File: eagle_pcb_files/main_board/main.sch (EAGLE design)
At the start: 19 parts

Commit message: Temporary version of main board
:')
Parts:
- added C1, C2, C3, C4, C5, C6, C7: (no value), rcl:C-EUC0402
- added U$3, U$9: POLOLU_FUEL_GAUGEBREAKBOARD, SparFun-FuelGauge:POLOLU_FUEL_GAUGEBREAKBOARD
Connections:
- net 3.3V: now also C1.2, C2.1, C3.1, C4.1, C5.2, C6.1, C7.1, U$3.VCC, U$9.VCC
- net B2: now also RAO2.GPIO6
- net GND: now also C1.1, C2.2, C3.2, C4.2, C5.1, C6.2, C7.2, U$3.-, U$3.GND, U$9.-, U$9.GND
- net SCL: now also U$3.SCL, U$9.SCL
- net SDA: now also U$3.SDA, U$9.SDA
- net VIN1: now also U$3.+
- net VIN2: now also U$9.+

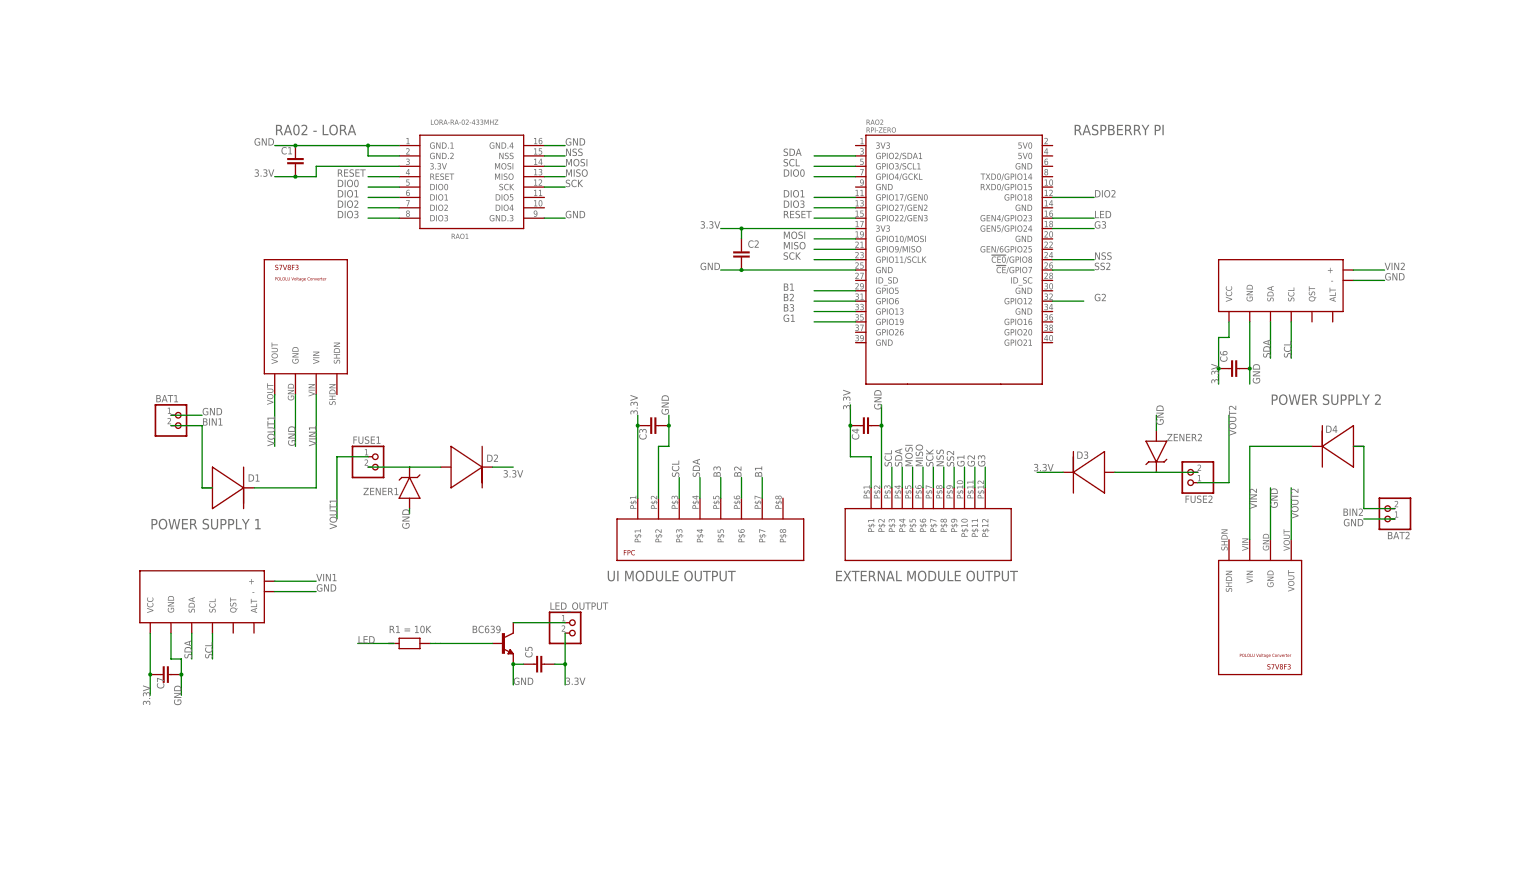
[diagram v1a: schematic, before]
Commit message: Bit better schematic
more readable
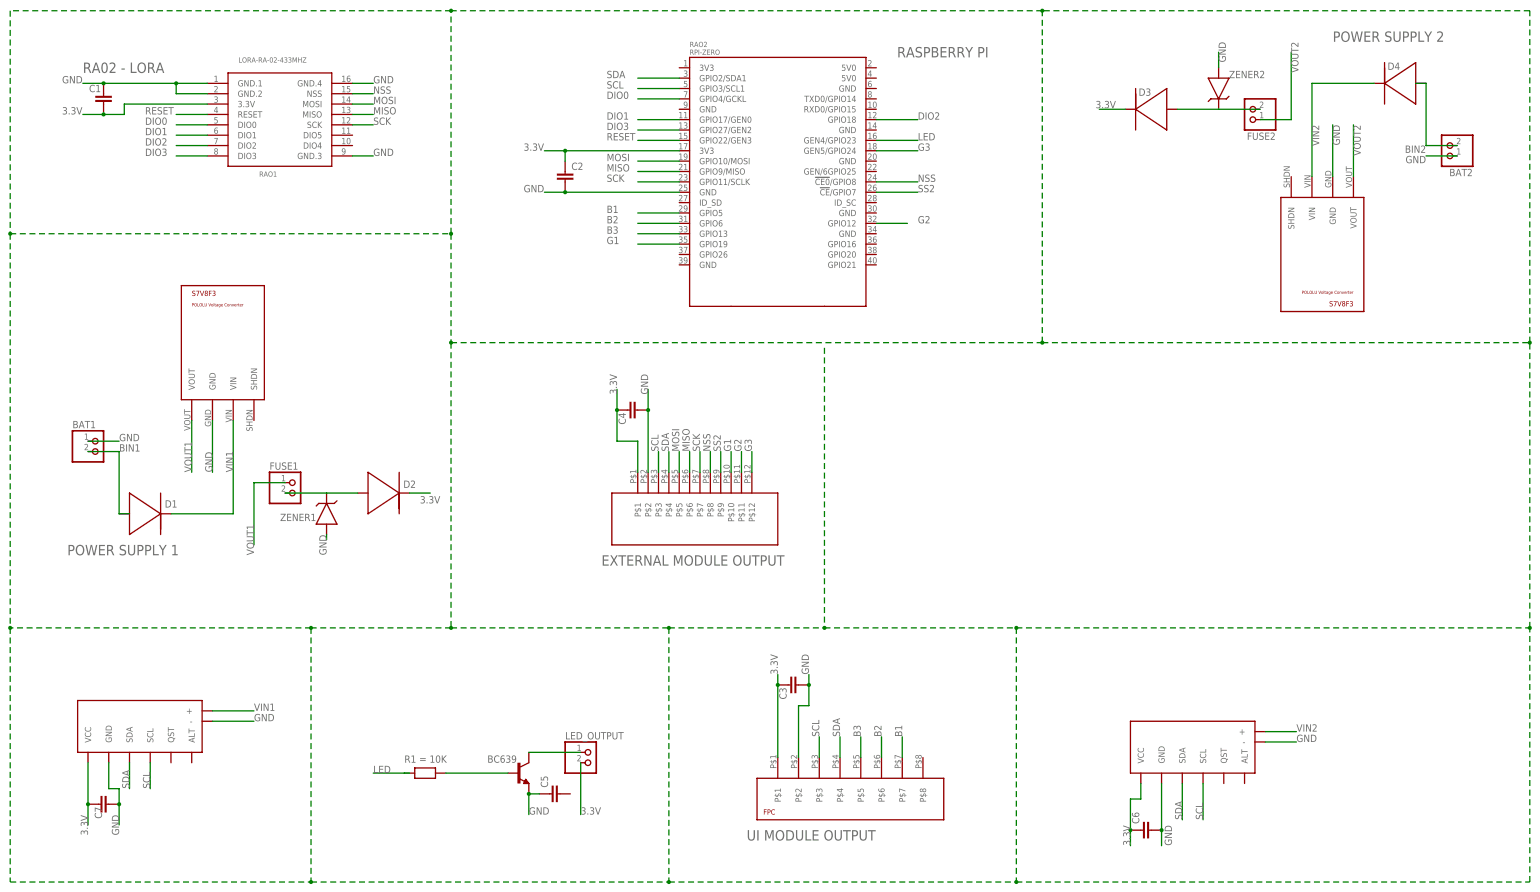
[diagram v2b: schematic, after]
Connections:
- net 3.3V: no longer C5.2
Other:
- moved on the sheet: BAT1, BAT2, BC639, C1, C2, C3, C4, C5, C6, C7, FUSE1, FUSE2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

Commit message: Better Schematic was so good, i've released sequel
better schematic
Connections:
- net 3.3V: now also C5.2
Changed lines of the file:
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@@
 <segment>
 <pinref part="LED_OUTPUT" gate="G$1" pin="2"/>
-<wire x1="44.45" y1="-80.01" x2="44.45" y2="-92.71" width="0.1524" layer="91"/>
+<wire x1="44.45" y1="-80.01" x2="44.45" y2="-87.63" width="0.1524" layer="91"/>
 <label x="44.45" y="-92.71" size="1.778" layer="95"/>
+<pinref part="C5" gate="G$1" pin="2"/>
+<wire x1="44.45" y1="-87.63" x2="44.45" y2="-92.71" width="0.1524" layer="91"/>
+<wire x1="41.91" y1="-87.63" x2="44.45" y2="-87.63" width="0.1524" layer="91" style="shortdash"/>
+<junction x="44.45" y="-87.63"/>
 </segment>
 <segment>

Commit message: jeez another schematic
Added fancy aesthetics
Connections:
- net 3.3V: no longer C5.2, LED_OUTPUT.2
- net VIN1: now also C5.2, LED_OUTPUT.2
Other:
- note added: "FUEL GAUGE 1"
- note added: "FUEL GAUGE 2"
- note added: "LED DRIVER"
- note added: "LORA RA-02"
- note added: "RASPBERRY PI ZERO"
- note removed: "RA02 - LORA"
- note removed: "RASPBERRY PI"
- moved on the sheet: C4
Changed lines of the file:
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@@
 <sheet>
 <plain>
-<text x="85.09" y="-99.06" size="2.54" layer="95">UI MODULE OUTPUT</text>
-<text x="-81.28" y="-29.21" size="2.54" layer="95">POWER SUPPLY 1</text>
-<text x="228.6" y="96.52" size="2.54" layer="95">POWER SUPPLY 2</text>
-<text x="121.92" y="92.71" size="2.54" layer="95">RASPBERRY PI</text>
-<text x="-77.47" y="88.9" size="2.54" layer="95">RA02 - LORA</text>
-<text x="49.53" y="-31.75" size="2.54" layer="95">EXTERNAL MODULE OUTPUT</text>
+<text x="-91.44" y="97.79" size="3.81" layer="91">LORA RA-02</text>
+<text x="-92.71" y="43.18" size="3.81" layer="91">POWER SUPPLY 1</text>
+<text x="-20.32" y="-53.34" size="3.81" layer="91">LED DRIVER</text>
+<text x="15.24" y="16.51" size="3.81" layer="91">EXTERNAL MODULE OUTPUT</text>
+<text x="67.31" y="-52.07" size="3.81" layer="91">UI MODULE OUTPUT</text>
+<text x="152.4" y="-52.07" size="3.81" layer="91">FUEL GAUGE 2</text>
+<text x="158.75" y="99.06" size="3.81" layer="91">POWER SUPPLY 2</text>
+<text x="13.97" y="99.06" size="3.81" layer="91">RASPBERRY PI ZERO</text>
+<text x="-93.98" y="-53.34" size="3.81" layer="91">FUEL GAUGE 1</text>
 </plain>
 <instances>
@@
 </instance>
 <instance part="U$1" gate="G$1" x="107.95" y="-88.9" smashed="yes"/>
-<instance part="U$2" gate="G$1" x="72.39" y="-21.59" smashed="yes"/>
+<instance part="U$2" gate="G$1" x="60.96" y="-25.4" smashed="yes"/>
 <instance part="BC639" gate="G$1" x="29.21" y="-82.55" smashed="yes">
 <attribute name="NAME" x="21.59" y="-80.01" size="1.778" layer="95"/>
@@
 <attribute name="VALUE" x="99.949" y="-59.436" size="1.778" layer="96" rot="R90"/>
 </instance>
-<instance part="C4" gate="G$1" x="55.88" y="6.35" smashed="yes" rot="R90">
-<attribute name="NAME" x="55.499" y="2.794" size="1.778" layer="95" rot="R90"/>
-<attribute name="VALUE" x="60.579" y="7.874" size="1.778" layer="96" rot="R90"/>
+<instance part="C4" gate="G$1" x="44.45" y="3.81" smashed="yes" rot="R90">
+<attribute name="NAME" x="44.069" y="0.254" size="1.778" layer="95" rot="R90"/>
+<attribute name="VALUE" x="49.149" y="5.334" size="1.778" layer="96" rot="R90"/>
 </instance>
 <instance part="C5" gate="G$1" x="36.83" y="-87.63" smashed="yes" rot="R90">
@@
 <segment>
 <pinref part="U$2" gate="G$1" pin="P$2"/>
-<label x="60.96" y="10.16" size="1.778" layer="95" rot="R90"/>
-<wire x1="60.96" y1="-8.89" x2="60.96" y2="6.35" width="0.1524" layer="91"/>
+<label x="49.53" y="7.62" size="1.778" layer="95" rot="R90"/>
+<wire x1="49.53" y1="-12.7" x2="49.53" y2="3.81" width="0.1524" layer="91"/>
 <pinref part="C4" gate="G$1" pin="2"/>
-<wire x1="60.96" y1="6.35" x2="60.96" y2="11.43" width="0.1524" layer="91"/>
-<junction x="60.96" y="6.35"/>
+<wire x1="49.53" y1="3.81" x2="49.53" y2="8.89" width="0.1524" layer="91"/>
+<junction x="49.53" y="3.81"/>
 </segment>
 <segment>
@@
 <segment>
 <pinref part="U$2" gate="G$1" pin="P$8"/>
-<wire x1="76.2" y1="-8.89" x2="76.2" y2="-3.81" width="0.1524" layer="91"/>
-<label x="76.2" y="-3.81" size="1.778" layer="95" rot="R90"/>
+<wire x1="64.77" y1="-12.7" x2="64.77" y2="-6.35" width="0.1524" layer="91"/>
+<label x="64.77" y="-6.35" size="1.778" layer="95" rot="R90"/>
 </segment>
 </net>
@@
 <segment>
 <pinref part="U$2" gate="G$1" pin="P$5"/>
-<wire x1="68.58" y1="-8.89" x2="68.58" y2="-3.81" width="0.1524" layer="91"/>
-<label x="68.58" y="-3.81" size="1.778" layer="95" rot="R90"/>
+<wire x1="57.15" y1="-12.7" x2="57.15" y2="-6.35" width="0.1524" layer="91"/>
+<label x="57.15" y="-6.35" size="1.778" layer="95" rot="R90"/>
 </segment>
 </net>
@@
 <segment>
 <pinref part="U$2" gate="G$1" pin="P$6"/>
-<wire x1="71.12" y1="-8.89" x2="71.12" y2="-3.81" width="0.1524" layer="91"/>
-<label x="71.12" y="-3.81" size="1.778" layer="95" rot="R90"/>
+<wire x1="59.69" y1="-12.7" x2="59.69" y2="-6.35" width="0.1524" layer="91"/>
+<label x="59.69" y="-6.35" size="1.778" layer="95" rot="R90"/>
 </segment>
 </net>
@@
 <wire x1="-45.72" y1="-67.31" x2="-35.56" y2="-67.31" width="0.1524" layer="91"/>
 <label x="-35.56" y="-67.31" size="1.778" layer="95"/>
+</segment>
+<segment>
+<pinref part="LED_OUTPUT" gate="G$1" pin="2"/>
+<wire x1="44.45" y1="-80.01" x2="44.45" y2="-87.63" width="0.1524" layer="91"/>
+<label x="44.45" y="-92.71" size="1.778" layer="95"/>
+<pinref part="C5" gate="G$1" pin="2"/>
+<wire x1="44.45" y1="-87.63" x2="44.45" y2="-92.71" width="0.1524" layer="91"/>
+<wire x1="41.91" y1="-87.63" x2="44.45" y2="-87.63" width="0.1524" layer="91"/>
+<junction x="44.45" y="-87.63"/>
 </segment>
 </net>
@@
 </segment>
 <segment>
-<pinref part="LED_OUTPUT" gate="G$1" pin="2"/>
-<wire x1="44.45" y1="-80.01" x2="44.45" y2="-87.63" width="0.1524" layer="91"/>
-<label x="44.45" y="-92.71" size="1.778" layer="95"/>
-<pinref part="C5" gate="G$1" pin="2"/>
-<wire x1="44.45" y1="-87.63" x2="44.45" y2="-92.71" width="0.1524" layer="91"/>
-<wire x1="41.91" y1="-87.63" x2="44.45" y2="-87.63" width="0.1524" layer="91" style="shortdash"/>
-<junction x="44.45" y="-87.63"/>
-</segment>
-<segment>
 <pinref part="U$2" gate="G$1" pin="P$1"/>
-<wire x1="58.42" y1="-8.89" x2="58.42" y2="-1.27" width="0.1524" layer="91"/>
-<label x="53.34" y="10.16" size="1.778" layer="95" rot="R90"/>
-<wire x1="58.42" y1="-1.27" x2="53.34" y2="-1.27" width="0.1524" layer="91"/>
+<wire x1="46.99" y1="-12.7" x2="46.99" y2="-3.81" width="0.1524" layer="91"/>
+<label x="41.91" y="7.62" size="1.778" layer="95" rot="R90"/>
+<wire x1="46.99" y1="-3.81" x2="41.91" y2="-3.81" width="0.1524" layer="91"/>
 <pinref part="C4" gate="G$1" pin="1"/>
-<wire x1="53.34" y1="-1.27" x2="53.34" y2="6.35" width="0.1524" layer="91"/>
-<wire x1="53.34" y1="6.35" x2="53.34" y2="11.43" width="0.1524" layer="91"/>
-<junction x="53.34" y="6.35"/>
+<wire x1="41.91" y1="-3.81" x2="41.91" y2="3.81" width="0.1524" layer="91"/>
+<wire x1="41.91" y1="3.81" x2="41.91" y2="8.89" width="0.1524" layer="91"/>
+<junction x="41.91" y="3.81"/>
 </segment>
 <segment>
@@
 <segment>
 <pinref part="U$2" gate="G$1" pin="P$7"/>
-<wire x1="73.66" y1="-8.89" x2="73.66" y2="-3.81" width="0.1524" layer="91"/>
-<label x="73.66" y="-3.81" size="1.778" layer="95" rot="R90"/>
+<wire x1="62.23" y1="-12.7" x2="62.23" y2="-6.35" width="0.1524" layer="91"/>
+<label x="62.23" y="-6.35" size="1.778" layer="95" rot="R90"/>
 </segment>
 </net>
@@
 <segment>
 <pinref part="U$2" gate="G$1" pin="P$3"/>
-<wire x1="63.5" y1="-8.89" x2="63.5" y2="-3.81" width="0.1524" layer="91"/>
-<label x="63.5" y="-3.81" size="1.778" layer="95" rot="R90"/>
+<wire x1="52.07" y1="-12.7" x2="52.07" y2="-6.35" width="0.1524" layer="91"/>
+<label x="52.07" y="-6.35" size="1.778" layer="95" rot="R90"/>
 </segment>
 <segment>
@@
 <segment>
 <pinref part="U$2" gate="G$1" pin="P$4"/>
-<wire x1="66.04" y1="-8.89" x2="66.04" y2="-3.81" width="0.1524" layer="91"/>
-<label x="66.04" y="-3.81" size="1.778" layer="95" rot="R90"/>
+<wire x1="54.61" y1="-12.7" x2="54.61" y2="-6.35" width="0.1524" layer="91"/>
+<label x="54.61" y="-6.35" size="1.778" layer="95" rot="R90"/>
 </segment>
 <segment>
@@
 <segment>
 <pinref part="U$2" gate="G$1" pin="P$9"/>
-<wire x1="78.74" y1="-8.89" x2="78.74" y2="-3.81" width="0.1524" layer="91"/>
-<label x="78.74" y="-3.81" size="1.778" layer="95" rot="R90"/>
+<wire x1="67.31" y1="-12.7" x2="67.31" y2="-6.35" width="0.1524" layer="91"/>
+<label x="67.31" y="-6.35" size="1.778" layer="95" rot="R90"/>
 </segment>
 </net>
@@
 <segment>
 <pinref part="U$2" gate="G$1" pin="P$10"/>
-<wire x1="81.28" y1="-8.89" x2="81.28" y2="-3.81" width="0.1524" layer="91"/>
-<label x="81.28" y="-3.81" size="1.778" layer="95" rot="R90"/>
+<wire x1="69.85" y1="-12.7" x2="69.85" y2="-6.35" width="0.1524" layer="91"/>
+<label x="69.85" y="-6.35" size="1.778" layer="95" rot="R90"/>
 </segment>
 <segment>
@@
 <segment>
 <pinref part="U$2" gate="G$1" pin="P$11"/>
-<wire x1="83.82" y1="-8.89" x2="83.82" y2="-3.81" width="0.1524" layer="91"/>
-<label x="83.82" y="-3.81" size="1.778" layer="95" rot="R90"/>
+<wire x1="72.39" y1="-12.7" x2="72.39" y2="-6.35" width="0.1524" layer="91"/>
+<label x="72.39" y="-6.35" size="1.778" layer="95" rot="R90"/>
 </segment>
 <segment>
@@
 <segment>
 <pinref part="U$2" gate="G$1" pin="P$12"/>
-<wire x1="86.36" y1="-8.89" x2="86.36" y2="-3.81" width="0.1524" layer="91"/>
-<label x="86.36" y="-3.81" size="1.778" layer="95" rot="R90"/>
-</segment>
-<segment>
+<wire x1="74.93" y1="-12.7" x2="74.93" y2="-6.35" width="0.1524" layer="91"/>
+<label x="74.93" y="-6.35" size="1.778" layer="95" rot="R90"/>
+</segment>
+<segment>
